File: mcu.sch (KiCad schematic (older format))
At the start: 54 parts, among them J1 AudioJack4, J3 Conn_01x06, J5 Conn_01x11, J7 Conn_01x06, SW2 SW_Push, U2 ATmega32U4, U4 IS31FL3737, X1 XRCGB16M000FXN00R0

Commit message: 4R updated placement of MCU
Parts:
- added LED_2: STATUS_LED, LED_SMD:LED_0603_1608Metric, symbol Device:LED_Small
- added R7: 33, Resistor_SMD:R_0603_1608Metric, symbol Device:R
- added SW1: Reset, SamacSys_Parts:EVPBB2A9B000, symbol Switch:SW_Push
- C1: value 0u1F -> 0u1; Fält4 6V3 -> 1; Manufacturer_Name (none) -> AVX; Manufacturer_Part_Number (none) -> 06035C104JAT2A; Mouser Part Number (none) -> 581-06035C104JAT2A
- C10: footprint Capacitor_SMD:C_0805_2012Metric_Pad1.15x1.40mm_HandSolder -> Capacitor_SMD:C_0805_2012Metric; Fält4 (none) -> 1; Manufacturer_Name (none) -> Samsung Electro-Mechanics; Manufacturer_Part_Number (none) -> CL21B105KBFNNNG; Mouser Part Number (none) -> 187-CL21B105KBFNNNG
- C11: footprint Capacitor_SMD:C_0805_2012Metric_Pad1.15x1.40mm_HandSolder -> Capacitor_SMD:C_0805_2012Metric; Fält4 (none) -> 1; Manufacturer_Name (none) -> TDK; Manufacturer_Part_Number (none) -> C2012X7R1H475K125AC; Mouser Part Number (none) -> 810-C2012X7R475K125C
- C12, C15, C18, C19, C2, C4, C7, C8, C9: Fält4 (none) -> 1; Manufacturer_Name (none) -> AVX; Manufacturer_Part_Number (none) -> 06035C104JAT2A; Mouser Part Number (none) -> 581-06035C104JAT2A
- C16, C20, C21, C22: Fält4 (none) -> 1; Manufacturer_Name (none) -> Taiyo Yuden; Manufacturer_Part_Number (none) -> UMK107B7474KA-TR; Mouser Part Number (none) -> 963-UMK107B7474KA-TR
- C17: footprint Capacitor_Tantalum_SMD:CP_EIA-3216-18_Kemet-A_Pad1.58x1.35mm_HandSolder -> Capacitor_Tantalum_SMD:CP_EIA-3216-18_Kemet-A; Fält4 (none) -> 1; Manufacturer_Name (none) -> AVX; Manufacturer_Part_Number (none) -> TPSA226K010T0900; Mouser Part Number (none) -> 581-TPSA226K010T0900
- C3: footprint Capacitor_Tantalum_SMD:CP_EIA-3216-18_Kemet-A_Pad1.58x1.35mm_HandSolder -> Capacitor_Tantalum_SMD:CP_EIA-3216-18_Kemet-A; Fält4 (none) -> 1; Manufacturer_Name (none) -> AVX; Manufacturer_Part_Number (none) -> TAJA106M010RNJ; Mouser Part Number (none) -> 581-TAJA106M010R
- C5, C6: Fält4 (none) -> 1; Manufacturer_Name (none) -> AVX; Manufacturer_Part_Number (none) -> 06035A220JAT2A; Mouser Part Number (none) -> 581-06035A220J
- F1: footprint Fuse:Fuse_0805_2012Metric_Pad1.15x1.40mm_HandSolder -> Fuse:Fuse_0603_1608Metric; Fält4 (none) -> 1; Manufacturer_Name (none) -> LittleFuse; Manufacturer_Part_Number (none) -> 04000025WR; Mouser Part Number (none) -> 576-04000025WR
- J1: value AudioJack4 -> TRRS; footprint Keyboard 2:TRRS-PJ-320A-reversible -> Keyboard Library:TRRS-PJ-320A-reversible; Fält4 (none) -> 1; Manufacturer_Part_Number (none) -> PJ-320A
- J3, J5, J7: Fält4 (none) -> 0; Manufacturer_Part_Number (none) -> Pinheader
- JP1, JP2, JP3, JP4, JP5, JP6: Fält4 (none) -> 0; Manufacturer_Part_Number (none) -> Jumper
- LED_1: renamed from POWER_LED1; value LED_Small -> PWR_LED; footprint LED_SMD:LED_0603_1608Metric_Pad1.05x0.95mm_HandSolder -> LED_SMD:LED_0603_1608Metric; Fält4 (none) -> 1; Manufacturer_Name (none) -> Kingbright; Manufacturer_Part_Number (none) -> APT1608EC; Mouser Part Number (none) -> 604-APT1608EC
- R1: Fält4 (none) -> 1; Manufacturer_Name (none) -> Panasonic; Manufacturer_Part_Number (none) -> ERJ-3EKF3300V; Mouser Part Number (none) -> 667-ERJ-3EKF3300V
- R10: Fält4 (none) -> 1; Manufacturer_Name (none) -> Panasonic; Manufacturer_Part_Number (none) -> ERJ-3GEYJ472V; Mouser Part Number (none) -> 667-ERJ-3GEYJ472V
- R11: Fält4 (none) -> 1; Manufacturer_Name (none) -> Panasonic; Manufacturer_Part_Number (none) -> ERJ-3EKF1002V; Mouser Part Number (none) -> 667-ERJ-3GEYJ103V
- R13: Fält4 (none) -> 1; Manufacturer_Name (none) -> Panasonic; Manufacturer_Part_Number (none) -> ERJ-3EKF33R0V; Mouser Part Number (none) -> 667-ERJ-3EKF33R0V
- R14: Fält4 (none) -> 1; Manufacturer_Name (none) -> Panasonic; Manufacturer_Part_Number (none) -> ERJ-3GEYJ203V; Mouser Part Number (none) -> 667-ERJ-3GEYJ203V
- R15, R16, R17: Fält4 (none) -> 1; Manufacturer_Name (none) -> Panasonic; Manufacturer_Part_Number (none) -> ERJ-3EKF1003V; Mouser Part Number (none) -> 667-ERJ-3EKF1003V
- R2, R3: Fält4 (none) -> 1; Manufacturer_Name (none) -> Panasonic; Manufacturer_Part_Number (none) -> ERJ-3EKF5101V; Mouser Part Number (none) -> 667-ERJ-3EKF5101V
- R4, R5: Fält4 (none) -> 1; Manufacturer_Name (none) -> Panasonic; Manufacturer_Part_Number (none) -> ERJ-3GEYJ220V; Mouser Part Number (none) -> 667-ERJ-3GEYJ220V
- R6: value 10K -> 10k; Fält4 (none) -> 1; Manufacturer_Name (none) -> Panasonic; Manufacturer_Part_Number (none) -> ERJ-3EKF1002V; Mouser Part Number (none) -> 667-ERJ-3GEYJ103V
- R9: value 4K7 -> 4k7; Fält4 (none) -> 1; Manufacturer_Name (none) -> Panasonic; Manufacturer_Part_Number (none) -> ERJ-3GEYJ472V; Mouser Part Number (none) -> 667-ERJ-3GEYJ472V
- SW2: value SW_Push -> Reset; footprint Keyboard Library:2-pin_reset_switch -> SamacSys_Parts:EVPBB2A9B000; Fält4 (none) -> 1; Manufacturer_Name (none) -> C&K Switches; Manufacturer_Part_Number (none) -> PTS635SH43LFS; Mouser Part Number (none) -> 611-PTS635SH43LFS
- U2: Fält4 (none) -> 1; Manufacturer_Name (none) -> Atmel; Manufacturer_Part_Number (none) -> ATMEGA32U4RC-MU; Mouser Part Number (none) -> 556-ATMEGA32U4RC-MU
- U4, X1: Fält4 (none) -> 1
- USB1: Fält4 (none) -> 1; Manufacturer_Name (none) -> HRO; Manufacturer_Part_Number (none) -> HRO-TYPE-C-31-M-14
- VR1, VR2: Fält4 (none) -> 1; Manufacturer_Name (none) -> Bourns; Manufacturer_Part_Number (none) -> CG0603MLC-05E
- ZD1: Fält4 (none) -> 1; Manufacturer_Name (none) -> Vishay; Manufacturer_Part_Number (none) -> SS1P3L-M3/84A; Mouser Part Number (none) -> 625-SS1P3L-M3/84A
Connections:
- net COL_TH1: now also U2.26 (PD6); no longer U2.25 (PD4)
- net COL_TH2: now also U2.27 (PD7); no longer U2.26 (PD6)
- net GND: now also SW2.2, R7.2, SW1.1; no longer SW2.1
- net I2C+: now also J1.R1; no longer J1.R2
- net I2C-: now also J1.R2; no longer J1.R1
- net RESET: now also SW2.1, SW1.2; no longer SW2.2
- net ROW_4: now also U2.25 (PD4); no longer U2.27 (PD7)
- net LED: now reaches U2.8 (PB0)
- net LED: now also LED_2.2 (A)
- new net: LED_2.1 (K), R7.1
- no-connect marks 9 -> 8
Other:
- moved on the sheet: JP3, JP4, VR1

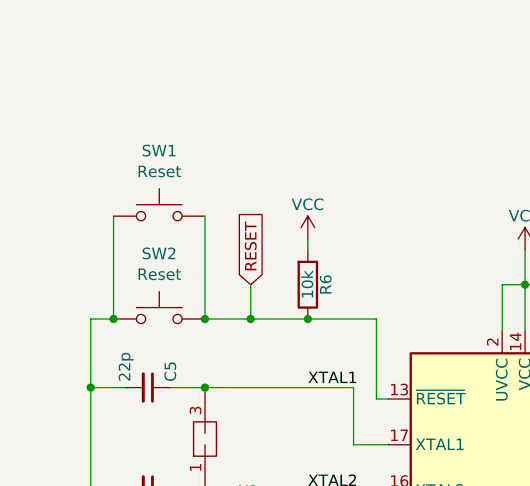
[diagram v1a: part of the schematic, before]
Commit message: fixed reset switch
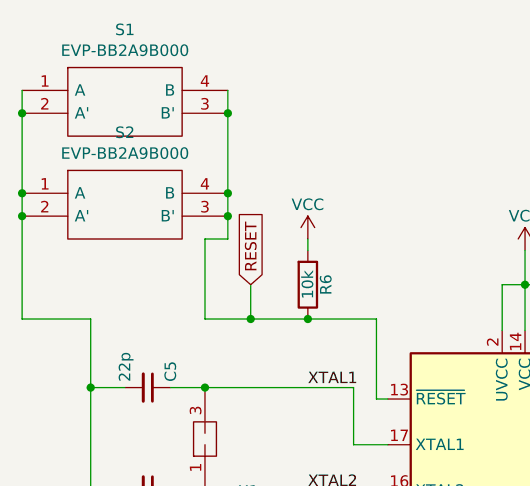
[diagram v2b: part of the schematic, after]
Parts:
- removed SW1, SW2: Reset, SamacSys_Parts:EVPBB2A9B000, symbol Switch:SW_Push
- added S1, S2: EVP-BB2A9B000, EVPBB2A9B000, symbol SamacSys_Parts:EVP-BB2A9B000
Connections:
- net GND: now also S1.1 (A), S1.2 (A'), S2.1 (A), S2.2 (A')
- net RESET: now also S1.3 (B'), S1.4 (B), S2.3 (B'), S2.4 (B)
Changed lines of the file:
@@
 	1    0    0    -1
 $EndComp
-Wire Wire Line
-	1000 1200 900  1200
 Text Notes 950  5250 0    50   ~ 0
 Recommended decouple: \n10uF per UVCC (4)\nand 0.1uF / VCC
@@
 	1    1850 1050
 	1    0    0    1
-$EndComp
-$Comp
-L Switch:SW_Push SW?
-U 1 1 5E61BB87
-P 1200 1200
-AR Path="/5E61BB87" Ref="SW?"  Part="1"
-AR Path="/5D6CC2CC/5E61BB87" Ref="SW?"  Part="1"
-AR Path="/5E135D8F/5E61BB87" Ref="SW2"  Part="1"
-F 0 "SW2" H 1200 1485 50  0000 C CNN
-F 1 "Reset" H 1200 1394 50  0000 C CNN
-F 2 "SamacSys_Parts:EVPBB2A9B000" H 1200 1400 50  0001 C CNN
-F 3 "~" H 1200 1400 50  0001 C CNN
-F 4 "1" H 1200 1200 50  0001 C CNN "Fält4"
-F 5 "C&K Switches" H 1200 1200 50  0001 C CNN "Manufacturer_Name"
-F 6 "PTS635SH43LFS" H 1200 1200 50  0001 C CNN "Manufacturer_Part_Number"
-F 7 "611-PTS635SH43LFS" H 1200 1200 50  0001 C CNN "Mouser Part Number"
-	1    1200 1200
-	-1   0    0    -1
 $EndComp
 Wire Wire Line
@@
 ROW_2
 NoConn ~ 3800 2950
-Wire Wire Line
-	900  1200 900  1500
 Wire Wire Line
 	2150 1200 2150 1550
@@
 Wire Wire Line
 	4250 1550 3400 1550
-$Comp
-L Switch:SW_Push SW?
-U 1 1 5FB99783
-P 1200 750
-AR Path="/5FB99783" Ref="SW?"  Part="1"
-AR Path="/5D6CC2CC/5FB99783" Ref="SW?"  Part="1"
-AR Path="/5E135D8F/5FB99783" Ref="SW1"  Part="1"
-F 0 "SW1" H 1200 1035 50  0000 C CNN
-F 1 "Reset" H 1200 944 50  0000 C CNN
-F 2 "SamacSys_Parts:EVPBB2A9B000" H 1200 950 50  0001 C CNN
-F 3 "~" H 1200 950 50  0001 C CNN
-F 4 "1" H 1200 750 50  0001 C CNN "Fält4"
-F 5 "C&K Switches" H 1200 750 50  0001 C CNN "Manufacturer_Name"
-F 6 "PTS635SH43LFS" H 1200 750 50  0001 C CNN "Manufacturer_Part_Number"
-F 7 "611-PTS635SH43LFS" H 1200 750 50  0001 C CNN "Mouser Part Number"
-	1    1200 750
-	1    0    0    -1
-$EndComp
-Wire Wire Line
-	1400 750  1400 1200
-Connection ~ 1400 1200
-Wire Wire Line
-	1000 1200 1000 750
-Connection ~ 1000 1200
 Text Label 3850 1550 0    50   ~ 0
 LED
+Wire Wire Line
+	900  1200 900  1500
+Wire Wire Line
+	1400 850  1400 1200
+$Comp
+L SamacSys_Parts:EVP-BB2A9B000 S1
+U 1 1 5F988CDD
+P 600 200
+F 0 "S1" H 1050 465 50  0000 C CNN
+F 1 "EVP-BB2A9B000" H 1050 374 50  0000 C CNN
+F 2 "EVPBB2A9B000" H 1350 300 50  0001 L CNN
+F 3 "https://industrial.panasonic.com/ac/cdn/e/control/switch/light-touch/catalog/sw_lt_eng_2616s.pdf" H 1350 200 50  0001 L CNN
+F 4 "Tactile Switches 2.6x1.6mm 1.6N 0.11mm travel IP67" H 1350 100 50  0001 L CNN "Description"
+F 5 "0" H 1350 0   50  0001 L CNN "Height"
+F 6 "667-EVP-BB2A9B000" H 1350 -100 50  0001 L CNN "Mouser Part Number"
+F 7 "https://www.mouser.co.uk/ProductDetail/Panasonic/EVP-BB2A9B000?qs=iHX4uCgIbgPa3HqgzZ6vLw%3D%3D" H 1350 -200 50  0001 L CNN "Mouser Price/Stock"
+F 8 "Panasonic" H 1350 -300 50  0001 L CNN "Manufacturer_Name"
+F 9 "EVP-BB2A9B000" H 1350 -400 50  0001 L CNN "Manufacturer_Part_Number"
+	1    600  200
+	1    0    0    -1
+$EndComp
+Wire Wire Line
+	1500 200  1500 300
+Wire Wire Line
+	1500 300  1500 650
+Wire Wire Line
+	1500 850  1400 850
+Connection ~ 1500 300
+Wire Wire Line
+	600  300  600  200
+Connection ~ 600  300
+$Comp
+L SamacSys_Parts:EVP-BB2A9B000 S2
+U 1 1 5FA2519E
+P 600 650
+F 0 "S2" H 1050 915 50  0000 C CNN
+F 1 "EVP-BB2A9B000" H 1050 824 50  0000 C CNN
+F 2 "EVPBB2A9B000" H 1350 750 50  0001 L CNN
+F 3 "https://industrial.panasonic.com/ac/cdn/e/control/switch/light-touch/catalog/sw_lt_eng_2616s.pdf" H 1350 650 50  0001 L CNN
+F 4 "Tactile Switches 2.6x1.6mm 1.6N 0.11mm travel IP67" H 1350 550 50  0001 L CNN "Description"
+F 5 "0" H 1350 450 50  0001 L CNN "Height"
+F 6 "667-EVP-BB2A9B000" H 1350 350 50  0001 L CNN "Mouser Part Number"
+F 7 "https://www.mouser.co.uk/ProductDetail/Panasonic/EVP-BB2A9B000?qs=iHX4uCgIbgPa3HqgzZ6vLw%3D%3D" H 1350 250 50  0001 L CNN "Mouser Price/Stock"
+F 8 "Panasonic" H 1350 150 50  0001 L CNN "Manufacturer_Name"
+F 9 "EVP-BB2A9B000" H 1350 50  50  0001 L CNN "Manufacturer_Part_Number"
+	1    600  650
+	1    0    0    -1
+$EndComp
+Wire Wire Line
+	600  650  600  300
+Wire Wire Line
+	1500 750  1500 850
+Connection ~ 600  750
+Wire Wire Line
+	600  650  600  750
+Connection ~ 600  650
+Wire Wire Line
+	1500 750  1500 650
+Connection ~ 1500 750
+Connection ~ 1500 650
+Wire Wire Line
+	900  1200 600  1200
+Wire Wire Line
+	600  750  600  1200
 $EndSCHEMATC
